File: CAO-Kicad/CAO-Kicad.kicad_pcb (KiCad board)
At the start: 2 copper layers, 100 x 100 mm, 18 parts, among them J1 ICSP, SW1 COMMUTATEUR A BILLE, U1 ATtiny85V-10P

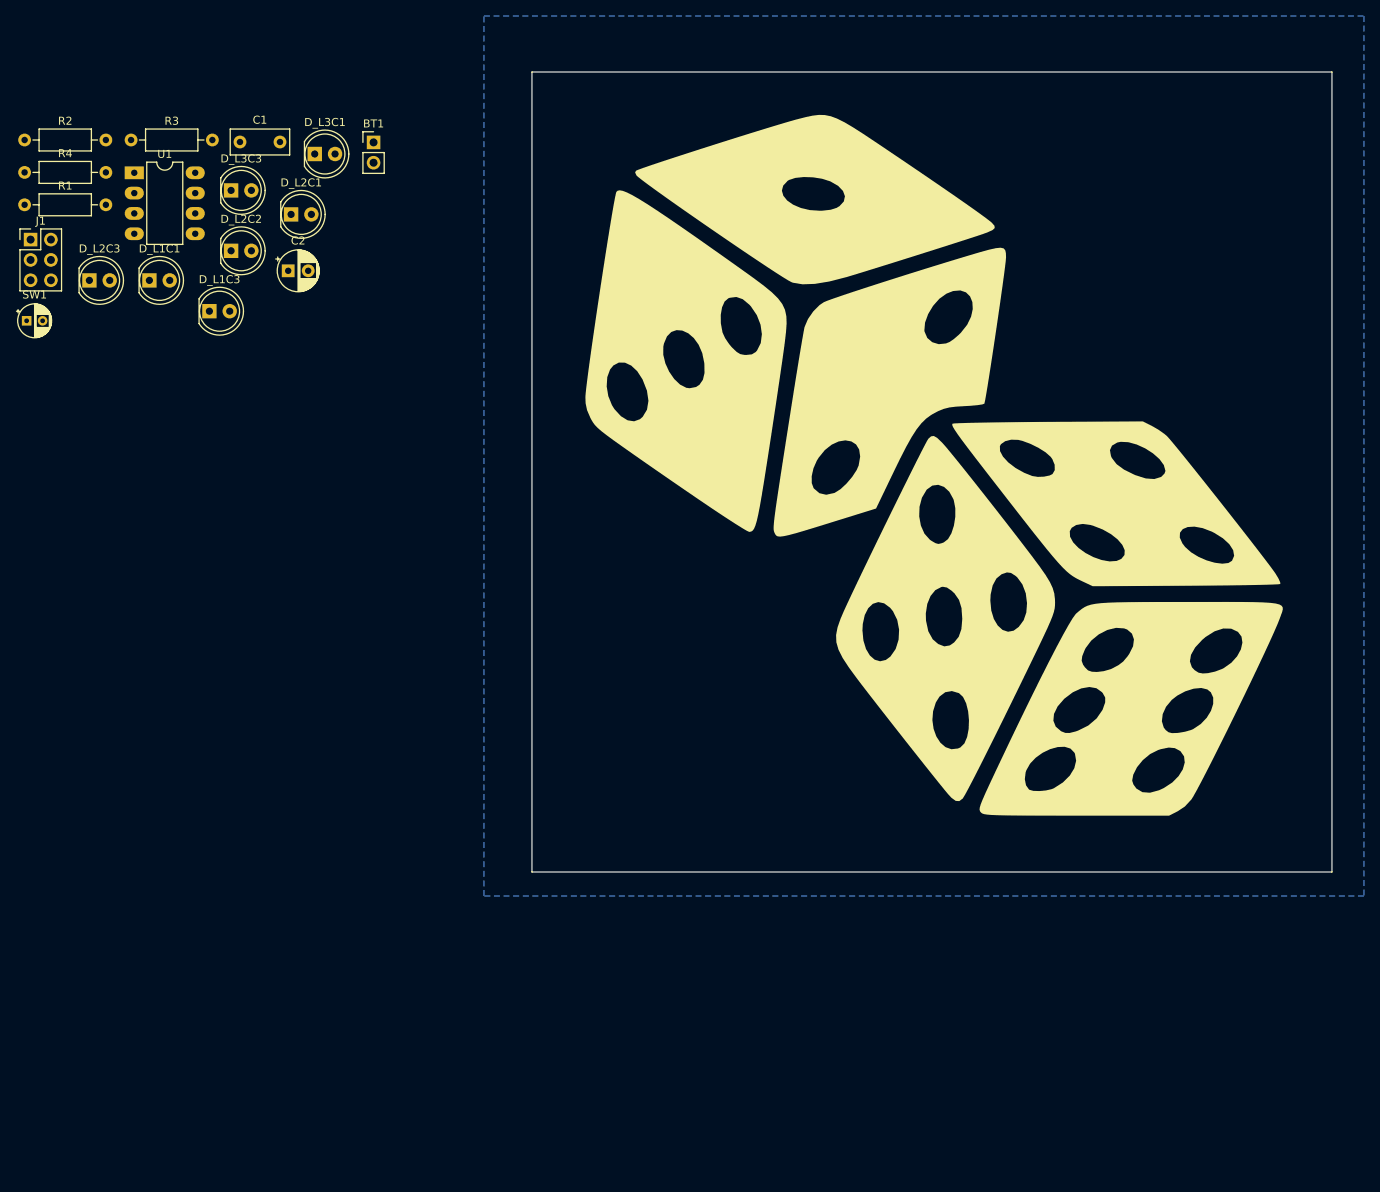
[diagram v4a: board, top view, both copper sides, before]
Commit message: MAJ pour la realiser un PCB de 40x40 mm
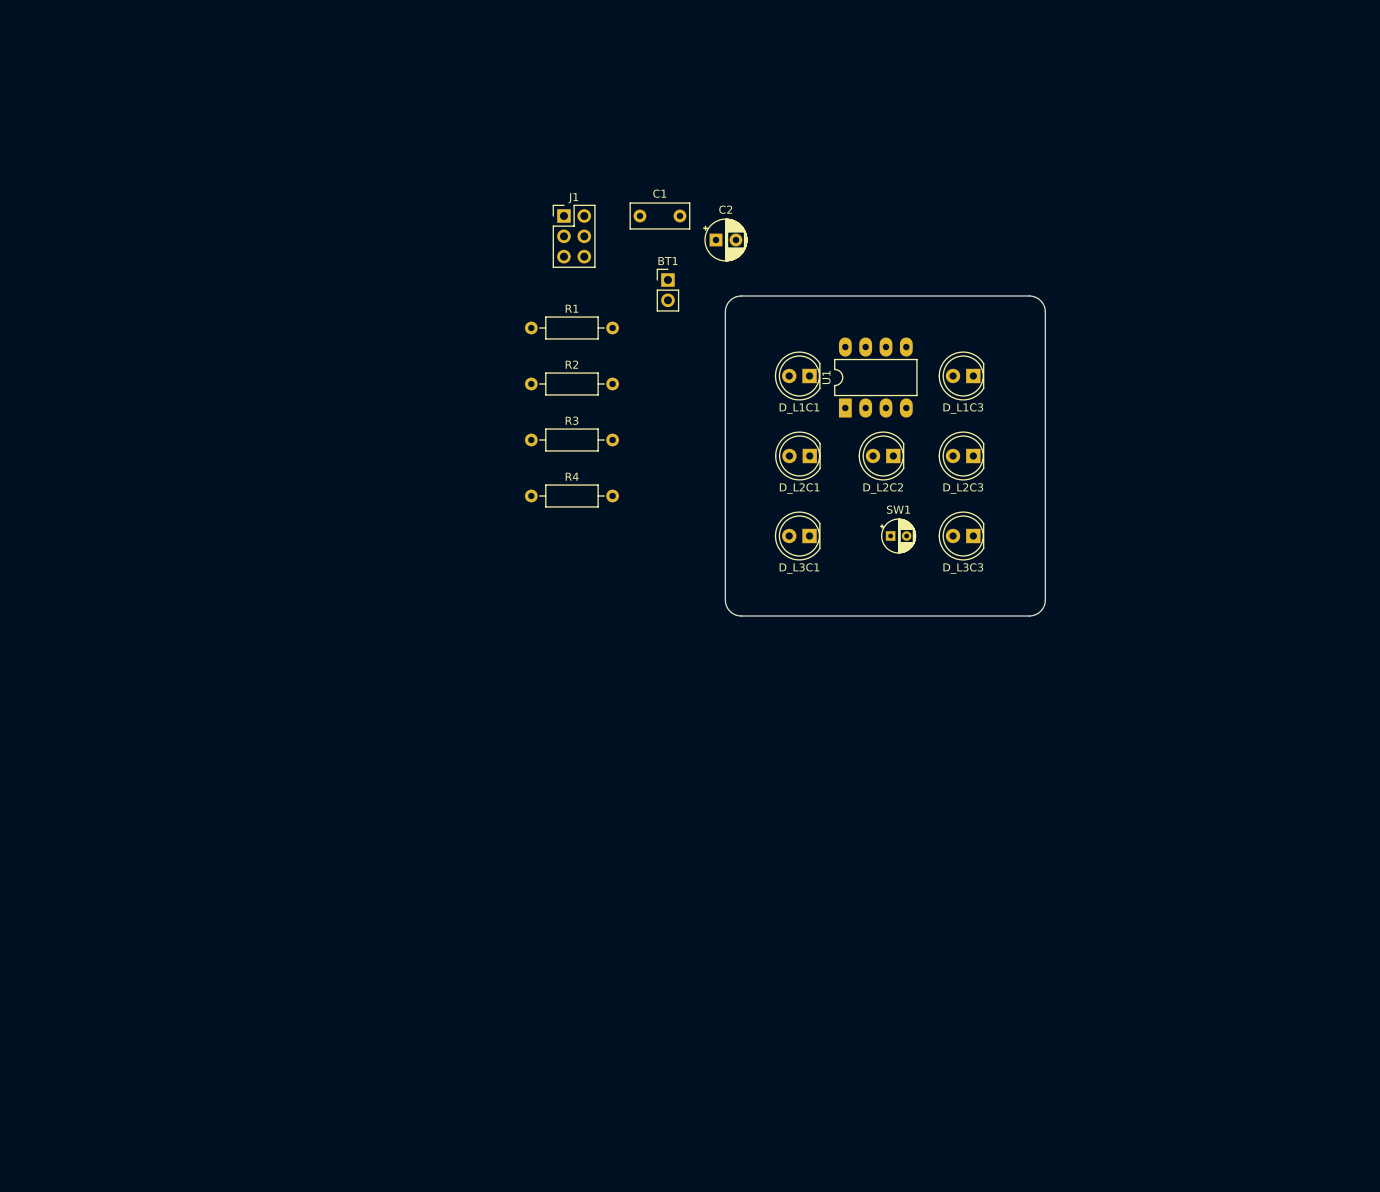
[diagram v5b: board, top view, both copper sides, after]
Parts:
- removed G***: LOGO, Image:image_de
- moved D_L2C3 112.7 mm to (151.2, 90.0), turned to 180 degrees
- moved SW1 111.3 mm to (140.8, 100.0)
- moved D_L3C3 102.3 mm to (151.2, 100.0), turned to 180 degrees
- moved D_L1C3 95.8 mm to (151.2, 80.0), turned to 180 degrees
- moved U1 93.6 mm to (135.2, 84.0), turned to 90 degrees
- moved D_L2C2 86.7 mm to (141.2, 90.0), turned to 180 degrees
- moved D_L1C1 83.4 mm to (130.7, 80.0), turned to 180 degrees
- moved D_L3C1 78.1 mm to (130.7, 100.0), turned to 180 degrees
- moved R4 75.2 mm to (95.9, 95.0)
- moved D_L2C1 71.5 mm to (130.7, 90.0), turned to 180 degrees
- moved R2 70.3 mm to (95.9, 81.0)
- moved J1 66.7 mm to (100.0, 60.0)
- moved R1 65.2 mm to (95.9, 74.0)
- moved R3 62.5 mm to (95.9, 88.0)
- moved C2 53.6 mm to (119.0, 63.0)
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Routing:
- removed copper zone on B.Cu, net (none)
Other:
- board size 100 x 100 mm -> 40 x 40 mm

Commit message: Routage de la carte electronique
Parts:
- BT1, J1: moved to B.Cu
- C1: value 100n -> 10u; footprint Capacitor_THT:C_Rect_L7.2mm_W3.0mm_P5.00mm_FKS2_FKP2_MKS2_MKP2 -> Capacitor_THT:CP_Radial_D5.0mm_P2.50mm; moved to B.Cu
- C2: value 10u -> 100n; footprint Capacitor_THT:CP_Radial_D5.0mm_P2.50mm -> Capacitor_THT:C_Rect_L7.2mm_W3.0mm_P5.00mm_FKS2_FKP2_MKS2_MKP2; moved to B.Cu
- R1: value 1k -> 560
- R3: value 560 -> 1k
- moved R1 48.6 mm to (142.8, 87.0), turned to 180 degrees
- moved R2 44.9 mm to (140.2, 73.4)
- moved J1 43.7 mm to (143.5, 64.1), turned to 90 degrees
- moved R3 39.4 mm to (134.8, 94.2)
- moved R4 38.9 mm to (134.8, 96.7)
- moved C2 24.5 mm to (136.5, 80.2)
- moved C1 24.3 mm to (129.4, 73.9), turned to -90 degrees
- moved BT1 12.8 mm to (124.4, 73.9), turned to 180 degrees
- moved SW1 0.29 mm to (141.1, 100.0)
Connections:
- net /De electronique/D_L2C1C3 renamed /D_L2C1C3
- net /De electronique/D_L3C1L1C3 renamed /D_L3C1L1C3
- net /De electronique/PB1/MISO renamed /PB1/MISO
- net /De electronique/PB2/SCK renamed /PB2/SCK
- net /De electronique/PB5/RESET renamed /PB5/RESET
- D_L1C1 pad 2: /De electronique/D_L1C1L3C3 -> /D_L1C1L3C3
- D_L2C2 pad 2: /De electronique/D_L2C2 -> /D_L2C2
- D_L3C3 pad 2: /De electronique/D_L1C1L3C3 -> /D_L1C1L3C3
- J1 pad 4: /De electronique/PB0/MOSI -> /PB0/MOSI
- R1 pad 1: /De electronique/CMD_L2C2 -> /PB0/MOSI
- R1 pad 2: /De electronique/D_L2C2 -> /D_L1C1L3C3
- R3 pad 1: /De electronique/PB0/MOSI -> /CMD_L2C2
- R3 pad 2: /De electronique/D_L1C1L3C3 -> /D_L2C2
- U1 pad 2: /De electronique/CMD_L2C2 -> /CMD_L2C2
- U1 pad 5: /De electronique/PB0/MOSI -> /PB0/MOSI
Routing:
- net /PB2/SCK: track 0.00 -> 82.8 mm
- net /D_L3C1L1C3: track 0.00 -> 80.1 mm, vias 0 -> 2
- net /D_L1C1L3C3: track 0.00 -> 47.9 mm, vias 0 -> 2
- net /D_L2C1C3: track 0.00 -> 31.1 mm
- net Net-(R4-Pad2): track 0.00 -> 21.0 mm
- net VCC: track 0.00 -> 16.1 mm
- net /PB0/MOSI: track 0.00 -> 15.0 mm
- net /CMD_L2C2: track 0.00 -> 12.6 mm
- net GND: track 0.00 -> 11.0 mm
- net /D_L2C2: track 0.00 -> 9.98 mm
- net /PB1/MISO: track 0.00 -> 2.99 mm
- added copper zone on B.Cu, net GND

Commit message: MAJ nommenclature
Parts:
- removed the J1 at (143.5, 64.1)
- added J2: ICSP, Connector_PinHeader_2.54mm:PinHeader_2x03_P2.54mm_Vertical, B.Cu at (148.7, 64.6)
- renumbered D_L1C1 to D1, D_L2C1 to D2, D_L3C1 to D3, D_L2C2 to D4, D_L1C3 to D5, D_L2C3 to D6, D_L3C3 to D7, BT1 to J1
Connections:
- net /D_L1C1L3C3 renamed /D_L1C1_L3C3
- net /D_L2C1C3 renamed /D_L2C1_L2C3
- net /D_L3C1L1C3 renamed /D_L3C1_L1C3
- net /PB0/MOSI renamed MOSI
- net /PB1/MISO renamed MISO
- net /PB2/SCK renamed SCK
- net Net-(R4-Pad2) renamed /CMD_L2C1_L2C3
- U1 pad 1: /PB5/RESET -> ~{RESET}
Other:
- board text added: "De-Electronique"
- board text added: "v1.0"

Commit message: Mise à jour du fichier README
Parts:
- removed J2: ICSP, Connector_PinHeader_2.54mm:PinHeader_2x03_P2.54mm_Vertical
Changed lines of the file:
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@@
   (setup
     (stackup
-      (layer "F.SilkS" (type "Top Silk Screen"))
+      (layer "F.SilkS" (type "Top Silk Screen") (color "White"))
       (layer "F.Paste" (type "Top Solder Paste"))
-      (layer "F.Mask" (type "Top Solder Mask") (color "Green") (thickness 0.01))
+      (layer "F.Mask" (type "Top Solder Mask") (color "Red") (thickness 0.01))
       (layer "F.Cu" (type "copper") (thickness 0.035))
       (layer "dielectric 1" (type "core") (thickness 1.51) (material "FR4") (epsilon_r 4.5) (loss_tangent 0.02))
       (layer "B.Cu" (type "copper") (thickness 0.035))
-      (layer "B.Mask" (type "Bottom Solder Mask") (color "Green") (thickness 0.01))
+      (layer "B.Mask" (type "Bottom Solder Mask") (color "Red") (thickness 0.01))
       (layer "B.Paste" (type "Bottom Solder Paste"))
-      (layer "B.SilkS" (type "Bottom Silk Screen"))
+      (layer "B.SilkS" (type "Bottom Silk Screen") (color "White"))
       (copper_finish "None")
       (dielectric_constraints no)
@@
     (aux_axis_origin 120.2 70)
     (pcbplotparams
-      (layerselection 0x0001000_fffffffe)
+      (layerselection 0x0000030_7ffffffe)
       (disableapertmacros false)
       (usegerberextensions false)
@@
       (sketchpadsonfab false)
       (subtractmaskfromsilk false)
-      (outputformat 1)
+      (outputformat 3)
       (mirror false)
       (drillshape 0)
@@
       (offset (xyz 0 0 0))
       (scale (xyz 1 1 1))
-      (rotate (xyz 0 0 0))
-    )
-  )
-  (footprint "Connector_PinHeader_2.54mm:PinHeader_2x03_P2.54mm_Vertical" (layer "B.Cu")
-    (at 148.7 64.6 -90)
-    (descr "Through hole straight pin header, 2x03, 2.54mm pitch, double rows")
-    (tags "Through hole pin header THT 2x03 2.54mm double row")
-    (property "Sheetfile" "CAO-Kicad.kicad_sch")
-    (property "Sheetname" "")
-    (attr through_hole)
-    (fp_text reference "J2" (at 1.27 2.33 90) (layer "B.SilkS")
-      (effects (font (size 1 1) (thickness 0.15)) (justify mirror))
-    )
-    (fp_text value "ICSP" (at 1.27 -7.41 90) (layer "B.Fab")
-      (effects (font (size 1 1) (thickness 0.15)) (justify mirror))
-    )
-    (fp_text user "${REFERENCE}" (at 1.27 -2.54) (layer "B.Fab")
-      (effects (font (size 1 1) (thickness 0.15)) (justify mirror))
-    )
-    (fp_line (start 1.27 -1.27) (end 1.27 1.33) (layer "B.SilkS") (width 0.12))
-    (fp_line (start -1.33 0) (end -1.33 1.33) (layer "B.SilkS") (width 0.12))
-    (fp_line (start 1.27 1.33) (end 3.87 1.33) (layer "B.SilkS") (width 0.12))
-    (fp_line (start -1.33 1.33) (end 0 1.33) (layer "B.SilkS") (width 0.12))
-    (fp_line (start -1.33 -1.27) (end -1.33 -6.41) (layer "B.SilkS") (width 0.12))
-    (fp_line (start -1.33 -1.27) (end 1.27 -1.27) (layer "B.SilkS") (width 0.12))
-    (fp_line (start -1.33 -6.41) (end 3.87 -6.41) (layer "B.SilkS") (width 0.12))
-    (fp_line (start 3.87 1.33) (end 3.87 -6.41) (layer "B.SilkS") (width 0.12))
-    (fp_line (start -1.8 -6.85) (end 4.35 -6.85) (layer "B.CrtYd") (width 0.05))
-    (fp_line (start -1.8 1.8) (end -1.8 -6.85) (layer "B.CrtYd") (width 0.05))
-    (fp_line (start 4.35 1.8) (end -1.8 1.8) (layer "B.CrtYd") (width 0.05))
-    (fp_line (start 4.35 -6.85) (end 4.35 1.8) (layer "B.CrtYd") (width 0.05))
-    (fp_line (start 3.81 1.27) (end 3.81 -6.35) (layer "B.Fab") (width 0.1))
-    (fp_line (start -1.27 -6.35) (end -1.27 0) (layer "B.Fab") (width 0.1))
-    (fp_line (start 0 1.27) (end 3.81 1.27) (layer "B.Fab") (width 0.1))
-    (fp_line (start 3.81 -6.35) (end -1.27 -6.35) (layer "B.Fab") (width 0.1))
-    (fp_line (start -1.27 0) (end 0 1.27) (layer "B.Fab") (width 0.1))
-    (pad "1" thru_hole rect locked (at 0 0 270) (size 1.7 1.7) (drill 1) (layers *.Cu *.Mask)
-      (net 8 "MISO") (pinfunction "Pin_1") (pintype "passive"))
-    (pad "2" thru_hole oval locked (at 2.54 0 270) (size 1.7 1.7) (drill 1) (layers *.Cu *.Mask)
-      (net 1 "VCC") (pinfunction "Pin_2") (pintype "passive"))
-    (pad "3" thru_hole oval locked (at 0 -2.54 270) (size 1.7 1.7) (drill 1) (layers *.Cu *.Mask)
-      (net 9 "SCK") (pinfunction "Pin_3") (pintype "passive"))
-    (pad "4" thru_hole oval locked (at 2.54 -2.54 270) (size 1.7 1.7) (drill 1) (layers *.Cu *.Mask)
-      (net 10 "MOSI") (pinfunction "Pin_4") (pintype "passive"))
-    (pad "5" thru_hole oval locked (at 0 -5.08 270) (size 1.7 1.7) (drill 1) (layers *.Cu *.Mask)
-      (net 11 "~{RESET}") (pinfunction "Pin_5") (pintype "passive"))
-    (pad "6" thru_hole oval locked (at 2.54 -5.08 270) (size 1.7 1.7) (drill 1) (layers *.Cu *.Mask)
-      (net 2 "GND") (pinfunction "Pin_6") (pintype "passive"))
-    (model "${KICAD6_3DMODEL_DIR}/Connector_PinHeader_2.54mm.3dshapes/PinHeader_2x03_P2.54mm_Vertical.wrl"
-      (offset (xyz 0 0 0))
-      (scale (xyz 1 1 1))
